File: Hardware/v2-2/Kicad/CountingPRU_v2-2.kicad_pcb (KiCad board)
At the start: 2 copper layers, 160 x 100 mm, 67 parts, among them J1 BBB, J2 IN_ETHERNET, J3 BERGOZ_02, J4 BERGOZ_01, P1 LNLS, Q1 BSR14, Q2 BSR14, Q3 BSR14, T1 Module-XFRMR-POE, T2 Transformer_1P_1S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

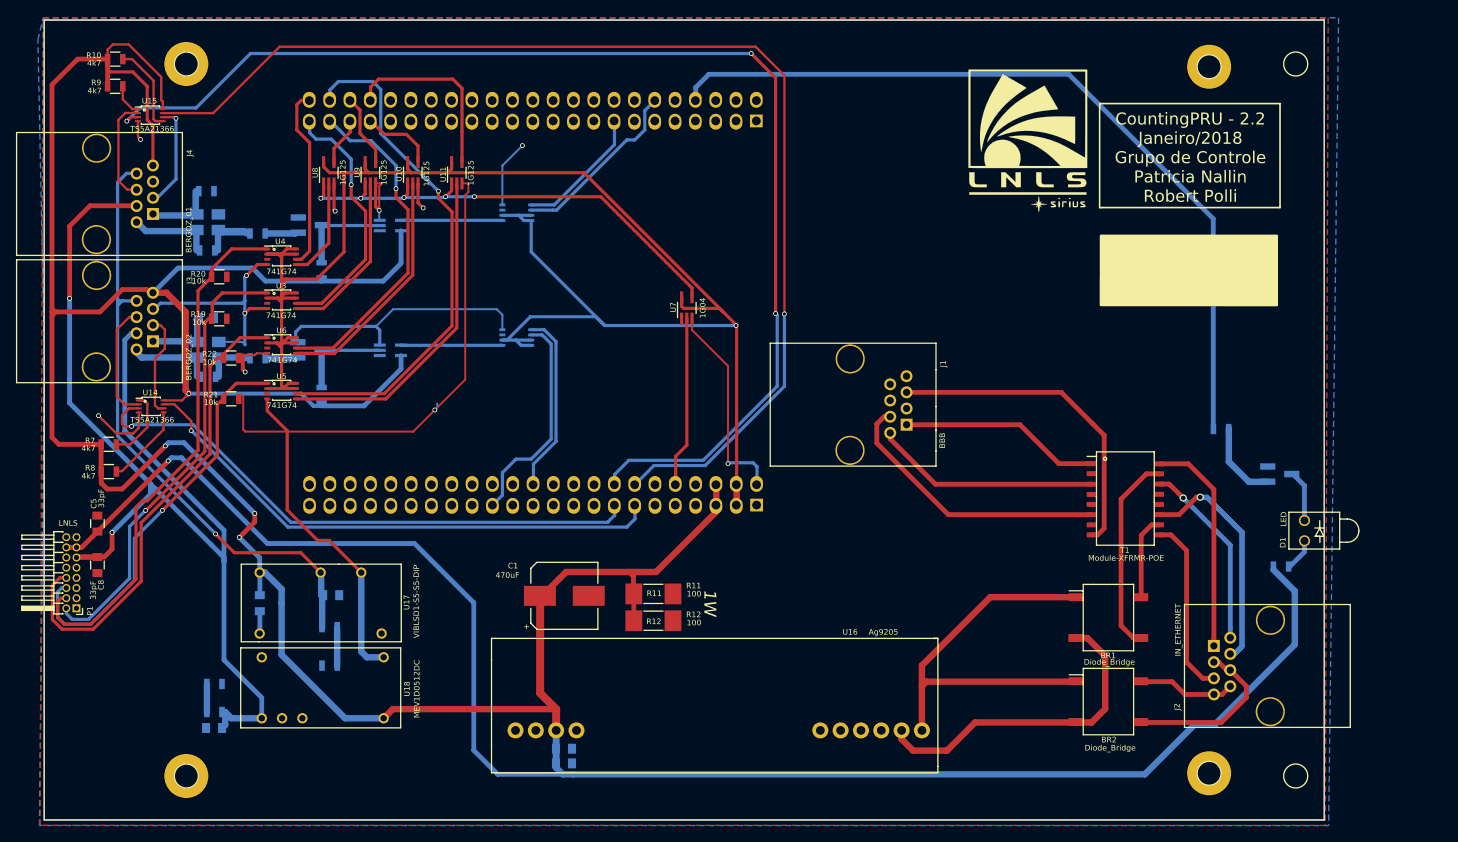
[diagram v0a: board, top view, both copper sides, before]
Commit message: Updating files for 2 LNLS connector
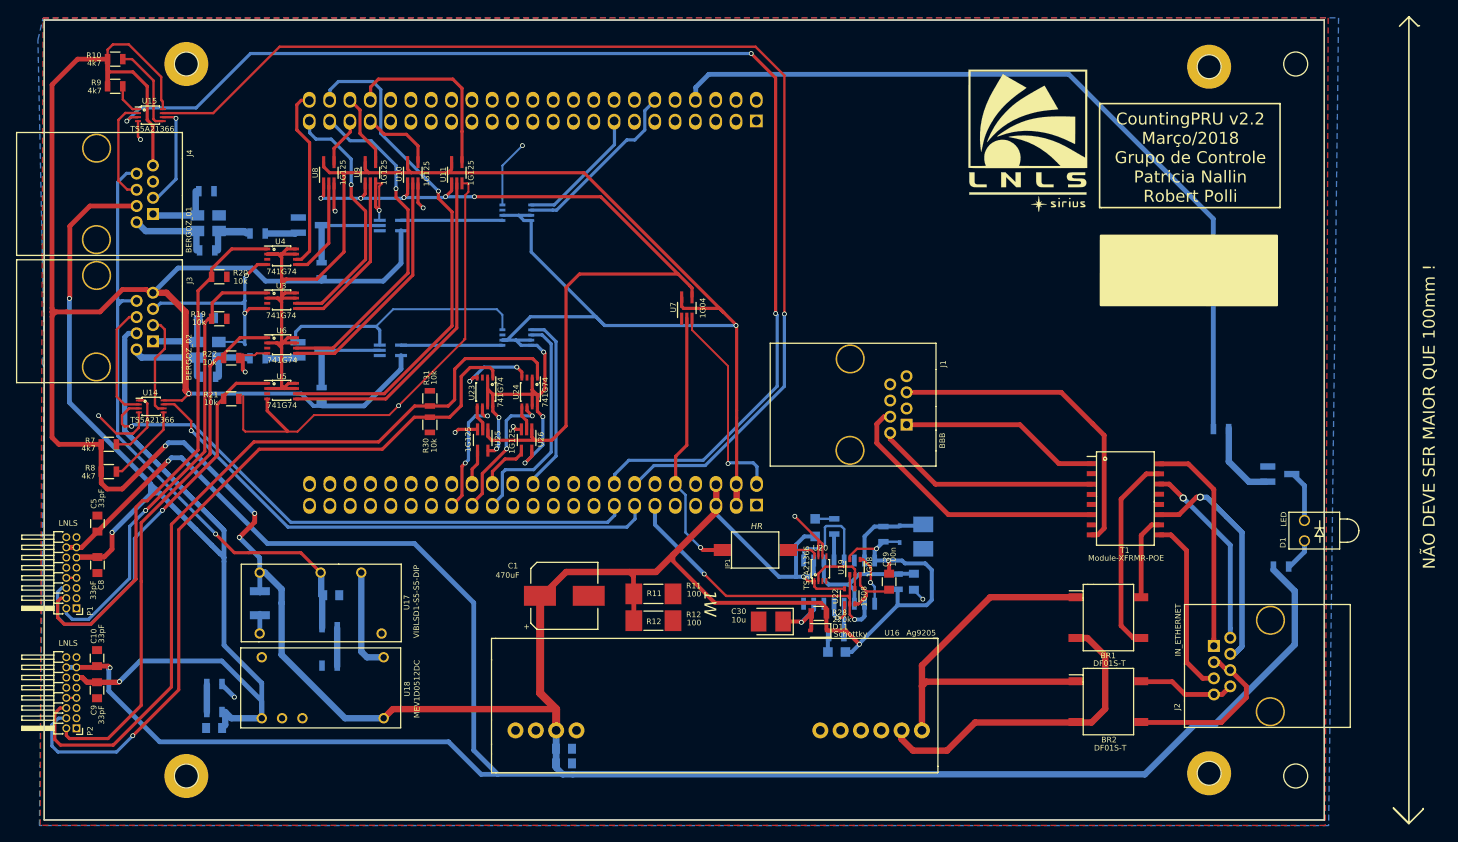
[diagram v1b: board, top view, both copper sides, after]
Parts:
- added C10: 33pF, Capacitors_SMD:C_0805, F.Cu at (37.9, 99.3)
- added C27: 100u, Capacitors_Tantalum_SMD:CP_Tantalum_Case-T_EIA-3528-12_Reflow, B.Cu at (141.2, 84.1)
- added C28: 100n, Capacitors_SMD:C_0805, B.Cu at (140.0, 89.7)
- added C29: 100n, Capacitors_SMD:C_0805, F.Cu at (136.9, 89.7)
- added C30: 10u, Capacitors_Tantalum_SMD:CP_Tantalum_Case-T_EIA-3528-12_Reflow, F.Cu at (122.2, 94.7)
- added C9: 33pF, Capacitors_SMD:C_0805, F.Cu at (37.9, 103.3)
- added D10: LED, LEDs:LED_0805, B.Cu at (130.4, 98.5)
- added D11: Schottky, Diodes_SMD:D_SOD-323, F.Cu at (128.1, 95.8)
- added D12: LED, LEDs:LED_0805, B.Cu at (127.7, 83.0)
- added D9: Schottky, Diodes_SMD:D_SOD-323, B.Cu at (138.3, 83.8)
- added JP1: HR, CONTROLE:DIPSwitchSMD_1pos, F.Cu at (124.3, 85.8)
- added P2: LNLS, Pin_Headers:Pin_Header_Angled_2x08_Pitch1.27mm, F.Cu at (35.4, 108.0)
- added R25: 910k, Resistors_SMD:R_0805, B.Cu at (136.2, 83.8)
- added R26: 330r, Resistors_SMD:R_0805, B.Cu at (130.3, 96.5)
- added R27: 10k, Resistors_SMD:R_0805, B.Cu at (138.0, 89.7)
- added R28: 220k, Resistors_SMD:R_0805, F.Cu at (128.1, 93.7)
- added R29: 330r, Resistors_SMD:R_0805, B.Cu at (130.1, 82.8)
- added R30: 10k, Resistors_SMD:R_0805, F.Cu at (79.5, 70.1)
- added R31: 10k, Resistors_SMD:R_0805, F.Cu at (79.5, 66.8)
- added U19: 1G08, TO_SOT_Packages_SMD:SOT-353_SC-70-5, F.Cu at (132.7, 87.9)
- added U20: TS5A21366, CONTROLE:VSSOP-8, F.Cu at (128.4, 88.1)
- added U21: 74LS123, Housings_SOIC:SOIC-16_3.9x9.9mm_Pitch1.27mm, B.Cu at (130.7, 89.8)
- added U22: 1G08, TO_SOT_Packages_SMD:SOT-353_SC-70-5, F.Cu at (132.0, 91.5)
- added U23: 741G74, CONTROLE:TSSOP-8, F.Cu at (86.4, 66.0)
- added U24: 741G74, CONTROLE:TSSOP-8, F.Cu at (92.0, 66.0)
- added U25: 1G125, TO_SOT_Packages_SMD:SOT-353_SC-70-5_Handsoldering, F.Cu at (86.1, 72.0)
- added U26: 1G125, TO_SOT_Packages_SMD:SOT-353_SC-70-5_Handsoldering, F.Cu at (91.6, 72.0)
- BR1, BR2: value Diode_Bridge -> DF01S-T
- C2: footprint Capacitors_SMD:C_0805 -> Capacitors_SMD:C_1210
- T2, T3: value Transformer_1P_1S -> CMC
- moved T3 0.15 mm to (47.7, 46.0)
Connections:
- net /AIN_01 renamed /Bergoz/AIN_01
- net /AIN_02 renamed /Bergoz/AIN_02
- net /BIN_01 renamed /Bergoz/BIN_01
- net /BIN_02 renamed /Bergoz/BIN_02
- net /D+_01 renamed /Bergoz/D+_01
- net /D+_02 renamed /Bergoz/D+_02
- net /D-_01 renamed /Bergoz/D-_01
- net /D-_02 renamed /Bergoz/D-_02
- net /SINAL_1 renamed /Bergoz/SINAL_1
- net /SINAL_2 renamed /Bergoz/SINAL_2
- Beagle1 pad C11: Net-(Beagle1-PadC11) -> /GPIO_RST
- Beagle1 pad C28: Net-(Beagle1-PadC28) -> /CONTA_8_BBB
- Beagle1 pad C29: Net-(Beagle1-PadC29) -> /CLEAR_8
- Beagle1 pad C30: Net-(Beagle1-PadC30) -> /CONTA_7_BBB
- Beagle1 pad C31: Net-(Beagle1-PadC31) -> /CLEAR_7
- J3 pad 3: /+24V -> /Bergoz/+24V
- J3 pad 8: /-5V -> /Bergoz/-5V
- J4 pad 3: /+24V -> /Bergoz/+24V
- J4 pad 8: /-5V -> /Bergoz/-5V
- P1 pad 8: /SINAL_6 -> GND
- U14 pad 3: /CH2 -> /Bergoz/CH2
- U14 pad 7: /CH1 -> /Bergoz/CH1
- U15 pad 3: /CH4 -> /Bergoz/CH4
- U15 pad 7: /CH3 -> /Bergoz/CH3
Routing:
- net +5V: track 563.4 -> 723.8 mm, vias 5 -> 10
- net /SINAL_8: track 0.00 -> 101.8 mm
- net /SINAL_7: track 0.00 -> 95.0 mm, vias 0 -> 1
- net /+24V: track 146.4 -> 216.0 mm, vias 2 -> 3
- net /~SYS_RST: track 60.8 -> 106.0 mm
- net +3V3: track 216.8 -> 259.7 mm, vias 1 -> 6
- net /GPIO_RST: track 0.00 -> 39.5 mm, vias 0 -> 2
- net /Bergoz/-5V: track 0.00 -> 36.9 mm
- net /-5V: track 77.6 -> 40.7 mm
- net /CLEAR_8: track 0.00 -> 17.3 mm, vias 0 -> 2
- net /HardReset_BBB/RST_RST: track 0.00 -> 17.2 mm
- net /CLEAR_7: track 0.00 -> 15.6 mm, vias 0 -> 2
- net GND: track 235.8 -> 249.9 mm, vias 11 -> 18
- net /HardReset_BBB/pulsoWAIT: track 0.00 -> 12.9 mm
- net /SYS_RST: track 22.5 -> 34.5 mm, vias 0 -> 1
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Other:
- board text added: "CountingPRU v2.2 Março/2018 Grupo de Controle Patricia Nallin Robert Polli"
- board text added: "NÃO DEVE SER MAIOR QUE 100mm !"
- board text removed: "CountingPRU - 2.2 Janeiro/2018 Grupo de Controle Patricia Nallin Robert Polli"

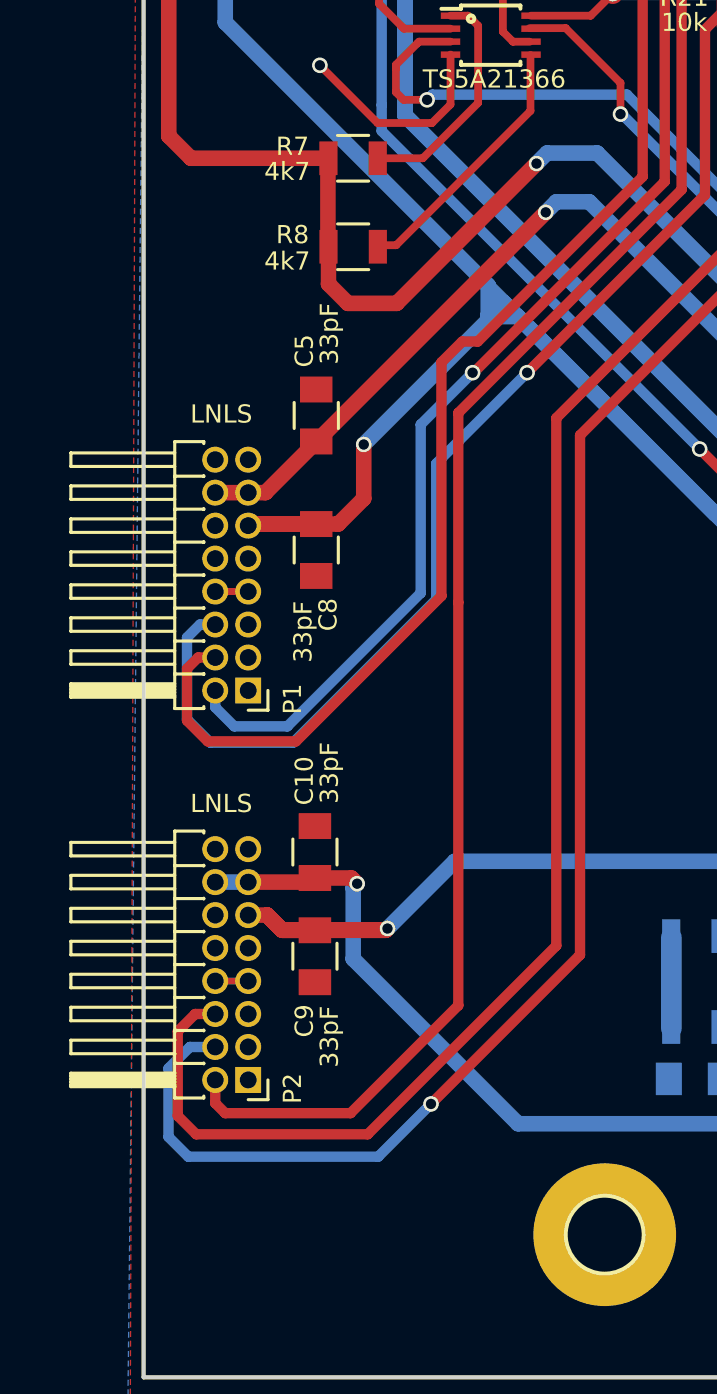
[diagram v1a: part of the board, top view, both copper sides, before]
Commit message: IOC files added and hardware v2-2 updated
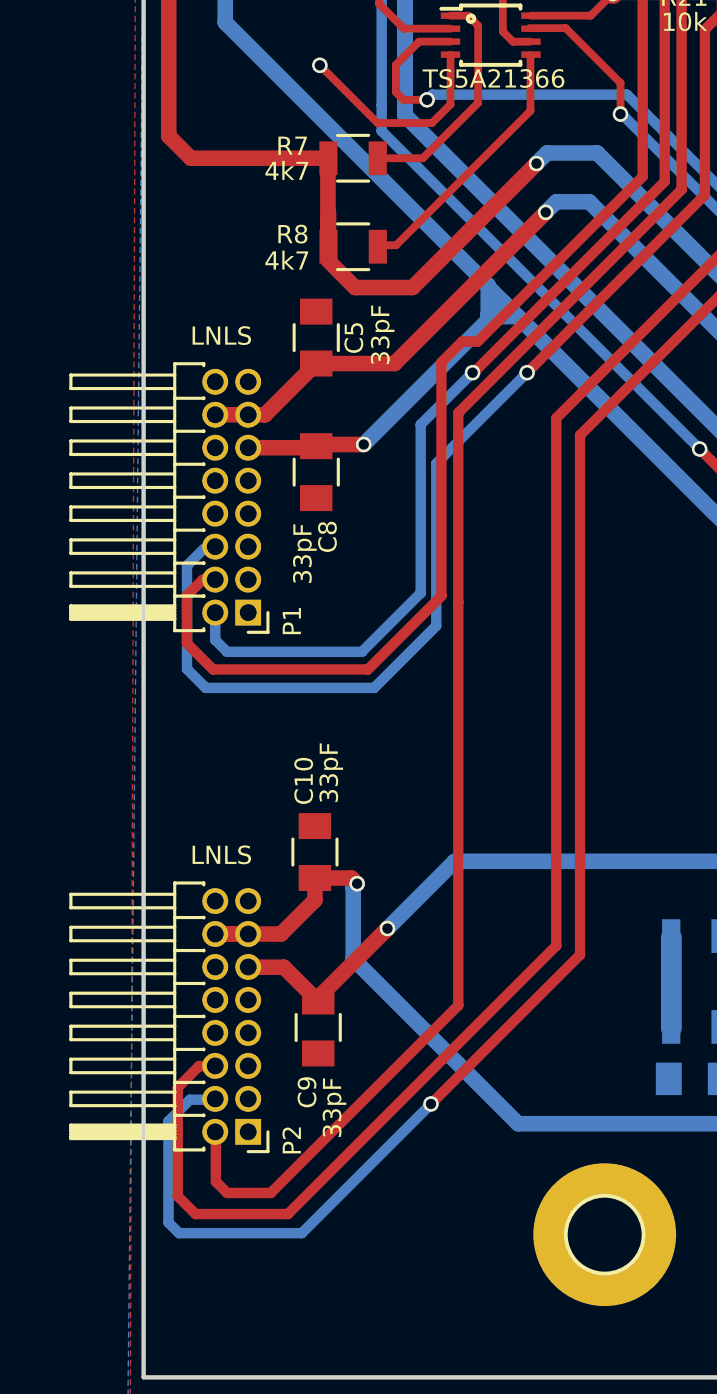
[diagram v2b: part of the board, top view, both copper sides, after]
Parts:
- moved C5 3.00 mm to (38.0, 79.4)
- moved C8 3.00 mm to (38.0, 84.6)
- moved P1 3.00 mm to (35.4, 90.0)
- moved C9 2.75 mm to (38.1, 106.0)
- moved P2 2.00 mm to (35.4, 110.0)
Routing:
- net /+24V: track 216.0 -> 205.6 mm
- net GND: track 249.9 -> 243.5 mm
- net +5V: track 723.8 -> 719.1 mm
- net /SINAL_7: track 95.0 -> 97.6 mm
- net /SINAL_6: track 66.6 -> 68.9 mm
- net /SINAL_8: track 101.8 -> 104.0 mm
- net /SINAL_4: track 66.9 -> 65.6 mm
- net /SINAL_3: track 57.4 -> 56.5 mm

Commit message: Update hardware files
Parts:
- R17: value 150 -> 180
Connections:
- net +3V3 renamed +3.3V
- C3 pad 1: /-5V -> -5V
- C4 pad 1: /+24V -> +24V
- C8 pad 1: /+24V -> +24V
- C9 pad 1: /+24V -> +24V
- J3 pad 3: /Bergoz/+24V -> +24V
- J3 pad 8: /Bergoz/-5V -> -5V
- J4 pad 3: /Bergoz/+24V -> +24V
- J4 pad 8: /Bergoz/-5V -> -5V
- P1 pad 11: /+24V -> +24V
- P2 pad 11: /+24V -> +24V
- R13 pad 1: /-5V -> -5V
- R15 pad 1: /+24V -> +24V
- U14 pad 3: /Bergoz/CH2 -> /CH2
- U14 pad 7: /Bergoz/CH1 -> /CH1
- U15 pad 3: /Bergoz/CH4 -> /CH4
- U15 pad 7: /Bergoz/CH3 -> /CH3
- U17 pad 11: /-5V -> -5V
- U18 pad 8: /+24V -> +24V
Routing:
- net +24V: track 0.00 -> 214.0 mm, vias 0 -> 3
- net /+24V: track 205.6 -> 0.00 mm, vias 3 -> 0
- net -5V: track 0.00 -> 77.6 mm, vias 0 -> 1
- net /-5V: track 40.7 -> 0.00 mm, vias 1 -> 0
- net /Bergoz/-5V: track 36.9 -> 0.00 mm
- net /SINAL_3: track 56.5 -> 83.5 mm
- net /SINAL_5: track 50.2 -> 66.5 mm
- net /Bergoz/+24V: track 6.86 -> 0.00 mm
- net /Bergoz/CH3: track 6.35 -> 0.00 mm
- net /CH3: track 138.9 -> 145.3 mm
- net /Bergoz/CH1: track 1.39 -> 0.00 mm
- net /CH1: track 67.0 -> 68.4 mm
- net /Bergoz/BIN_01: track 12.9 -> 14.2 mm
- net /CH2: track 70.8 -> 72.0 mm
- net /Bergoz/CH2: track 1.21 -> 0.00 mm
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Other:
- board text added: "CountingPRU v2.2 Abril/2018 Grupo de Controle Patricia Nallin Robert Polli"
- board text removed: "CountingPRU v2.2 Março/2018 Grupo de Controle Patricia Nallin Robert Polli"
